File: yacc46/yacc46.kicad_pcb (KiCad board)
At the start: 2 copper layers, 291.6 x 112.1 mm, 125 parts, among them J1 OLED_I2C, J2 GLOVE_I2C, SW1 SW_PUSH, SW10 SW_PUSH, SW11 SW_PUSH, SW12 SW_PUSH, SW13 SW_PUSH, SW14 SW_PUSH, SW15 SW_PUSH, SW16 SW_PUSH, SW17 SW_PUSH, SW18 SW_PUSH, SW19 Rotary_Encoder_Switch, SW2 SW_PUSH, SW20 SW_PUSH, SW21 SW_PUSH, SW22 SW_PUSH, SW23 SW_PUSH, SW24 SW_PUSH, SW25 SW_PUSH, SW26 SW_PUSH, SW27 SW_PUSH, SW28 SW_PUSH, SW29 SW_PUSH, SW3 SW_PUSH, SW30 SW_PUSH, SW31 SW_PUSH, SW32 SW_PUSH, SW33 SW_PUSH, SW34 SW_PUSH, SW35 SW_PUSH, SW36 Rotary_Encoder_Switch, SW37 SW_PUSH, SW38 SW_PUSH, SW39 SW_PUSH, SW4 SW_PUSH, SW40 SW_PUSH, SW41 SW_PUSH, SW42 SW_PUSH, SW43 SW_PUSH, SW44 SW_PUSH, SW45 SW_PUSH, SW46 SW_PUSH, SW47 SW_Push, SW5 SW_PUSH, SW6 SW_PUSH, SW7 SW_PUSH, SW8 SW_PUSH, SW9 SW_PUSH, U1 ProMicro_r

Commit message: flip right hand side's diodes direction
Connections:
- SW24 pad 1: COL5 -> Net-(D24-Pad1)
- SW24 pad 2: Net-(D24-Pad1) -> COL5
- SW25 pad 1: COL4 -> Net-(D25-Pad1)
- SW25 pad 2: Net-(D25-Pad1) -> COL4
- SW26 pad 1: COL3 -> Net-(D26-Pad1)
- SW26 pad 2: Net-(D26-Pad1) -> COL3
- SW27 pad 1: COL2 -> Net-(D27-Pad1)
- SW27 pad 2: Net-(D27-Pad1) -> COL2
- SW28 pad 1: COL1 -> Net-(D28-Pad1)
- SW28 pad 2: Net-(D28-Pad1) -> COL1
- SW29 pad 1: COL6 -> Net-(D29-Pad1)
- SW29 pad 2: Net-(D29-Pad1) -> COL6
- SW30 pad 1: COL5 -> Net-(D30-Pad1)
- SW30 pad 2: Net-(D30-Pad1) -> COL5
- SW31 pad 1: COL4 -> Net-(D31-Pad1)
- SW31 pad 2: Net-(D31-Pad1) -> COL4
- SW32 pad 1: COL3 -> Net-(D32-Pad1)
- SW32 pad 2: Net-(D32-Pad1) -> COL3
- SW33 pad 1: COL2 -> Net-(D33-Pad1)
- SW33 pad 2: Net-(D33-Pad1) -> COL2
- SW34 pad 1: COL1 -> Net-(D34-Pad1)
- SW34 pad 2: Net-(D34-Pad1) -> COL1
- SW35 pad 1: COL0 -> Net-(D35-Pad1)
- SW35 pad 2: Net-(D35-Pad1) -> COL0
- SW36 pad S1: COL6 -> Net-(D36-Pad1)
- SW36 pad S2: Net-(D36-Pad1) -> COL6
- SW37 pad 1: COL5 -> Net-(D37-Pad1)
- SW37 pad 2: Net-(D37-Pad1) -> COL5
- SW38 pad 1: COL4 -> Net-(D38-Pad1)
- SW38 pad 2: Net-(D38-Pad1) -> COL4
- SW39 pad 1: COL3 -> Net-(D39-Pad1)
- SW39 pad 2: Net-(D39-Pad1) -> COL3
- SW40 pad 1: COL2 -> Net-(D40-Pad1)
- SW40 pad 2: Net-(D40-Pad1) -> COL2
- SW41 pad 1: COL1 -> Net-(D41-Pad1)
- SW41 pad 2: Net-(D41-Pad1) -> COL1
- SW42 pad 1: COL0 -> Net-(D42-Pad1)
- SW42 pad 2: Net-(D42-Pad1) -> COL0
- SW43 pad 1: COL6 -> Net-(D43-Pad1)
- SW43 pad 2: Net-(D43-Pad1) -> COL6
- SW44 pad 1: COL5 -> Net-(D44-Pad1)
- SW44 pad 2: Net-(D44-Pad1) -> COL5
- SW45 pad 1: COL4 -> Net-(D45-Pad1)
- SW45 pad 2: Net-(D45-Pad1) -> COL4
- SW46 pad 1: COL3 -> Net-(D46-Pad1)
- SW46 pad 2: Net-(D46-Pad1) -> COL3

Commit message: modify diode positions
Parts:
- moved D34 9.48 mm to (287.2, 76.3), turned to 0 degrees
- moved D35 9.48 mm to (306.2, 71.6), turned to 0 degrees
- moved D41 9.48 mm to (287.2, 95.4), turned to 0 degrees
- moved D42 9.48 mm to (306.2, 90.6), turned to 0 degrees
- moved D28 9.48 mm to (287.2, 57.3), turned to 0 degrees
- moved D13 9.48 mm to (33.8, 90.6), turned to 0 degrees
- moved D6 9.48 mm to (33.8, 71.6), turned to 0 degrees
- moved D22 9.48 mm to (141.0, 118.7), turned to 334 degrees
- moved D23 9.48 mm to (117.0, 129.5), turned to 342 degrees
- moved D21 9.48 mm to (122.9, 111.4), turned to 342 degrees
- moved D11 9.48 mm to (131.9, 73.1), turned to 350 degrees
- moved D18 9.48 mm to (128.6, 91.8), turned to 350 degrees
- moved D5 9.48 mm to (135.2, 54.3), turned to 350 degrees
- moved D17 9.48 mm to (110.2, 86.2), turned to 350 degrees
- moved D10 9.48 mm to (113.5, 67.4), turned to 350 degrees
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
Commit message: modify led positions
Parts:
- moved LED13 23.8 mm to (225.9, 32.1)
- moved LED2 23.8 mm to (114.1, 32.1)
- moved LED11 17.9 mm to (305.7, 91.3)
- moved LED4 17.9 mm to (34.3, 91.3)
- moved LED12 6.81 mm to (275.0, 43.3)
- moved LED3 6.81 mm to (65.0, 43.3)
- moved LED1 3.00 mm to (148.4, 33.8)
- moved LED14 3.00 mm to (191.6, 33.8)
- moved LED9 2.12 mm to (229.8, 110.0), turned to 10 degrees
- moved LED6 2.12 mm to (110.2, 110.0), turned to 350 degrees
- moved LED10 1.47 mm to (264.1, 95.0)
- moved LED5 1.47 mm to (76.0, 95.0)
- moved LED7 0.76 mm to (147.4, 126.0)
- moved LED8 0.76 mm to (192.6, 126.0)

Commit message: modify PCB design rules
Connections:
- net Net-(JP1-Pad2) renamed /LED_POWER

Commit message: partially wired
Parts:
- moved D36 16.0 mm to (190.3, 81.7)
- moved D19 16.0 mm to (149.7, 81.8)
- moved D13 14.5 mm to (33.8, 76.2)
- moved D42 14.5 mm to (306.2, 76.2)
- moved D45 14.4 mm to (233.2, 92.5)
- moved D20 14.4 mm to (106.3, 92.5)
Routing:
- net /LED_POWER: track 0.00 -> 694.2 mm, vias 0 -> 4
- net ROW2: track 0.00 -> 366.8 mm, vias 0 -> 2
- net ROW1: track 0.00 -> 317.0 mm
- net ROW3: track 0.00 -> 224.6 mm, vias 0 -> 4
- net COL3: track 0.00 -> 213.8 mm, vias 0 -> 2
- net ROW0: track 0.00 -> 195.6 mm
- net COL4: track 0.00 -> 126.7 mm
- net COL5: track 0.00 -> 122.0 mm
- net COL2: track 0.00 -> 79.1 mm
- net COL1: track 0.00 -> 77.8 mm
- net Net-(LED3-Pad2): track 0.00 -> 71.4 mm, vias 0 -> 2
- net Net-(LED11-Pad2): track 0.00 -> 70.3 mm, vias 0 -> 2
- net SDA: track 0.00 -> 65.3 mm, vias 0 -> 1
- net SCL: track 0.00 -> 60.3 mm, vias 0 -> 1
- net Net-(LED4-Pad2): track 0.00 -> 57.7 mm
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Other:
- board text added: "RESET"

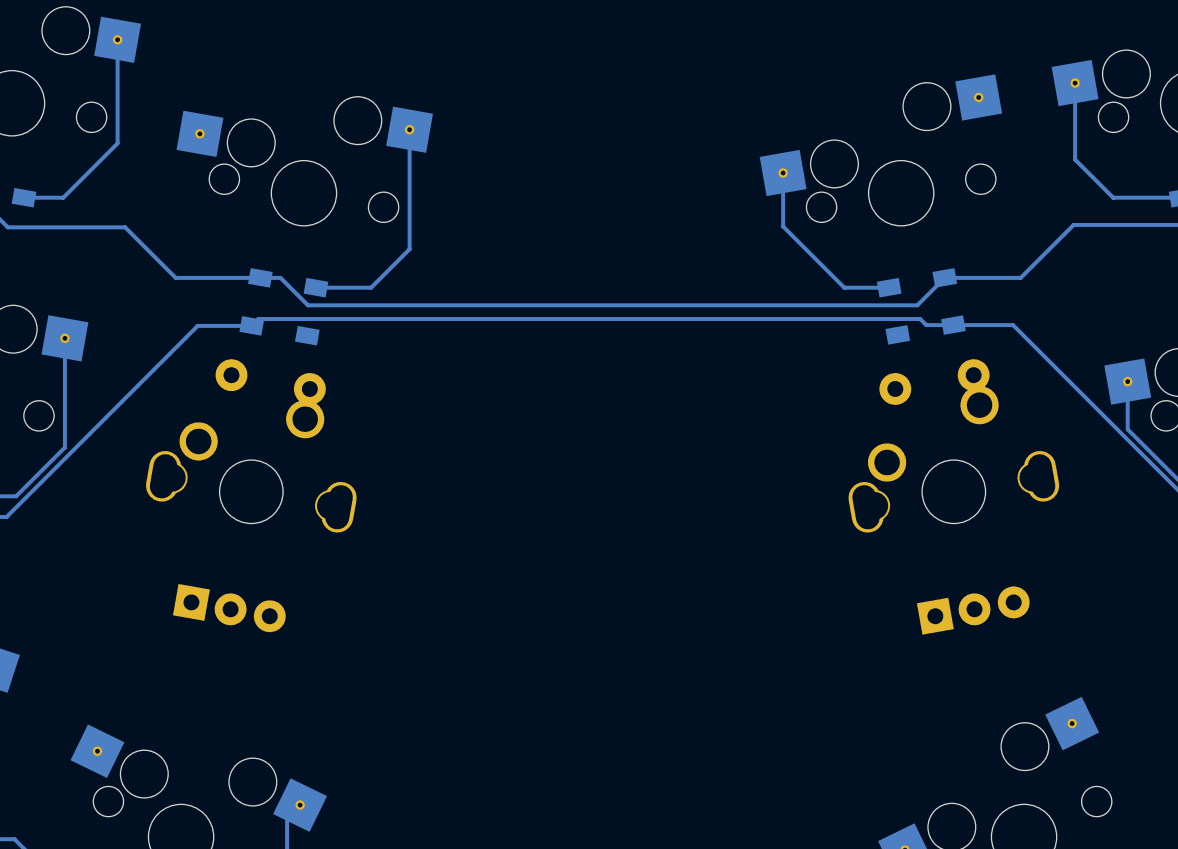
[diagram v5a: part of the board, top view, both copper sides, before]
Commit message: modify footprint of rotary encoders (use hot-swap socket)
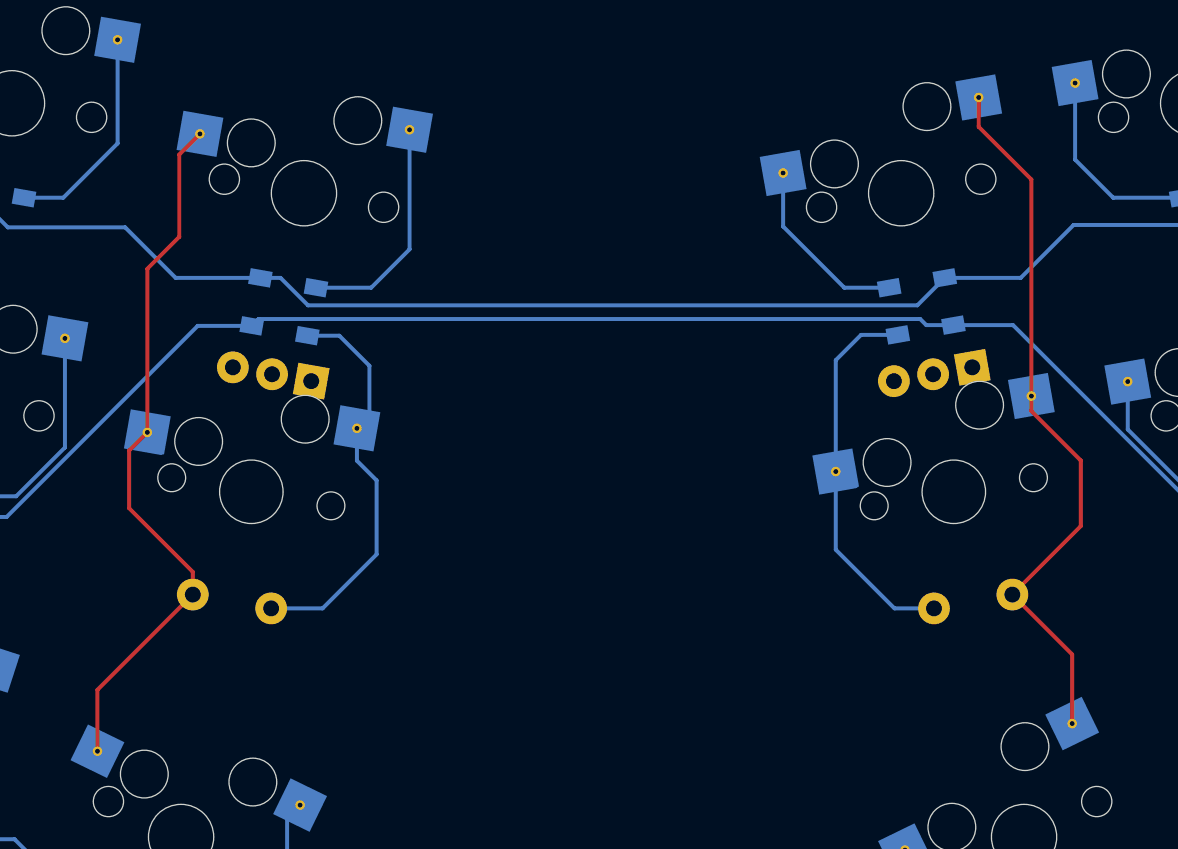
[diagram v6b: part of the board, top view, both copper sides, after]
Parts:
- SW19, SW36: footprint 1m38_kbd:RotaryEncoder_Alps_EC11E-and-CherryMX-Single -> 1m38_kbd:RotaryEncoder_Alps_EC11E-and-CherryMX-Hotswap
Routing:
- net COL6: track 0.00 -> 90.1 mm
- net Net-(D19-Pad2): track 0.00 -> 25.4 mm
- net Net-(D36-Pad1): track 0.00 -> 24.2 mm

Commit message: modify hole positions
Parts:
- moved H3 0.92 mm to (42.5, 94.8)
- moved H10 0.92 mm to (297.6, 94.8)
- moved H4 0.60 mm to (34.7, 46.9)
- moved H9 0.60 mm to (305.3, 46.9)
- moved H8 0.16 mm to (253.7, 29.1)
- moved H5 0.16 mm to (86.3, 29.1)

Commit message: wire PCB
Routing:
- net GND: track 32.2 -> 828.1 mm, vias 0 -> 14
- net COL0: track 38.9 -> 398.2 mm, vias 0 -> 1
- net COL1: track 77.8 -> 392.5 mm, vias 0 -> 1
- net COL2: track 79.1 -> 336.5 mm, vias 0 -> 1
- net COL3: track 213.8 -> 420.0 mm, vias 2 -> 3
- net COL4: track 126.7 -> 288.5 mm, vias 0 -> 1
- net COL5: track 122.0 -> 241.5 mm, vias 0 -> 1
- net ROW0: track 195.6 -> 301.1 mm
- net COL6: track 90.1 -> 166.3 mm, vias 0 -> 1
- net ROW3: track 224.6 -> 297.1 mm, vias 4 -> 5
- net VCC: track 46.4 -> 103.9 mm
- net ENCR1: track 0.00 -> 52.3 mm
- net ENCL2: track 0.00 -> 46.3 mm, vias 0 -> 1
- net ENCL1: track 0.00 -> 45.9 mm
- net ENCR2: track 0.00 -> 44.8 mm
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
